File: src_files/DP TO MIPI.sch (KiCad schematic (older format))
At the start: 20 parts

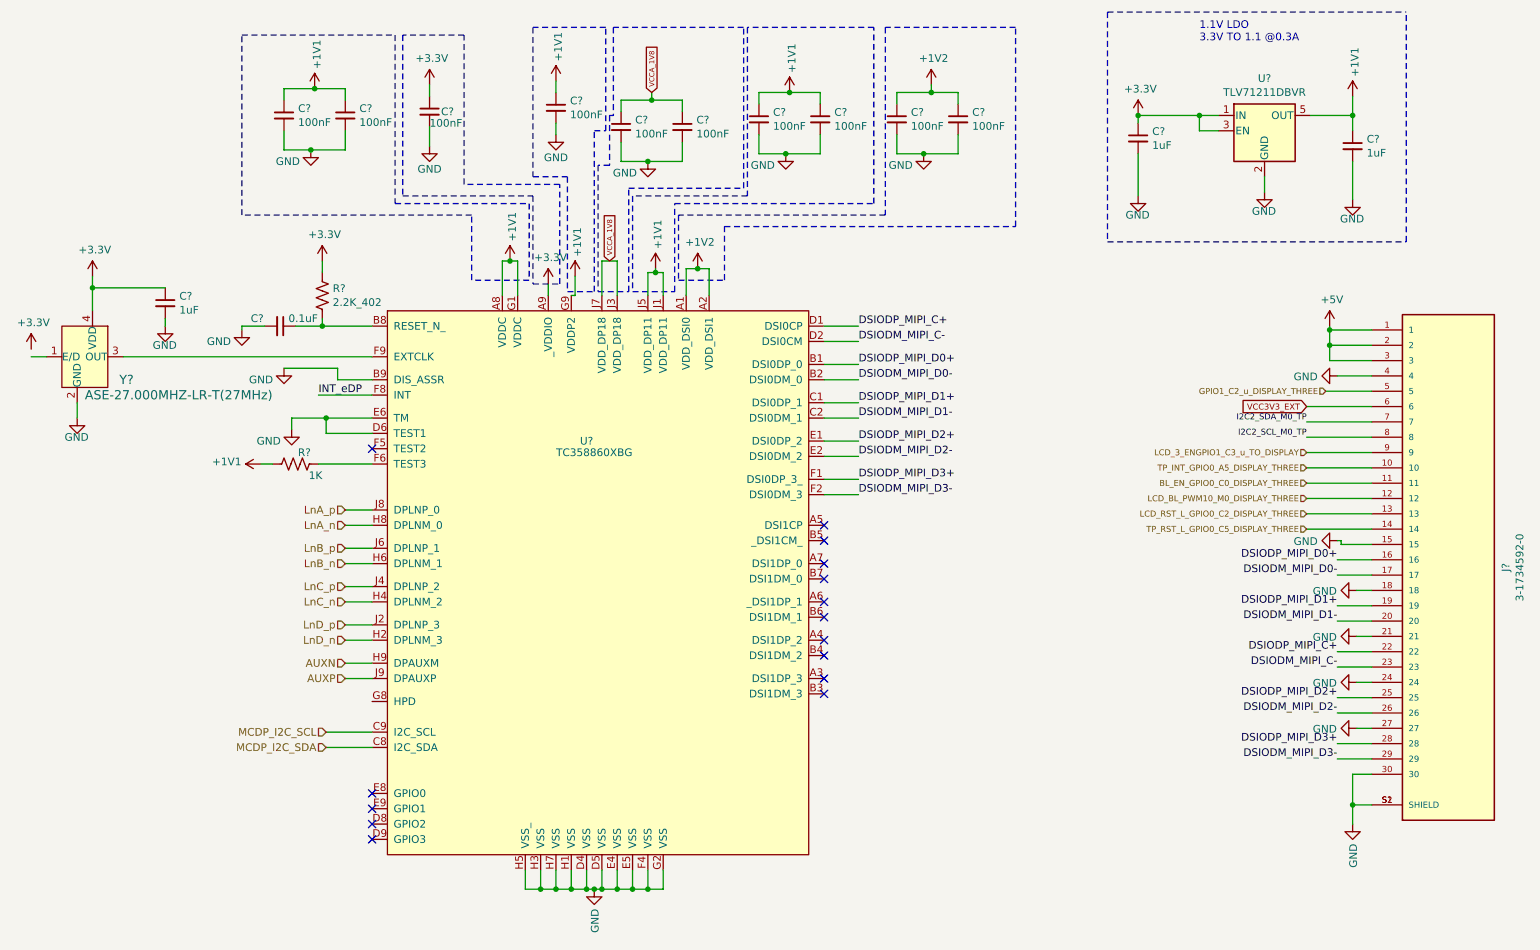
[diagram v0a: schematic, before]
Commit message: complete update on schematic and all display interfaces
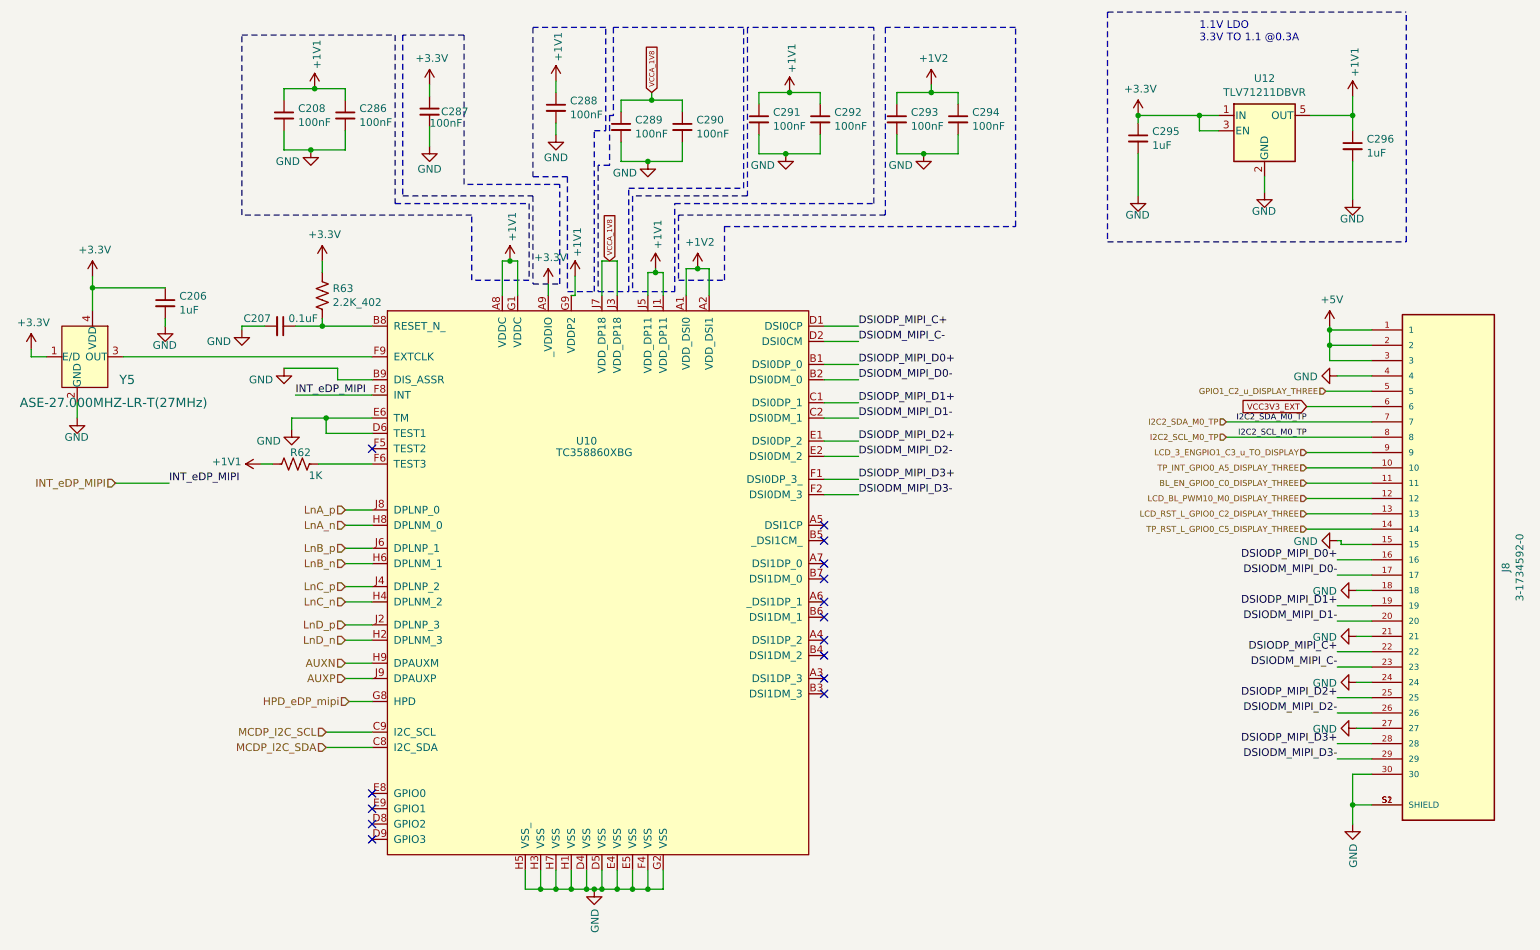
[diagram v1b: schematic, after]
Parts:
- gave numbers to parts that had none: 20
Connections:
- net +3V3: now also Y5.1 (E/D)
- net HPD_eDP_mipi: now reaches U10.G8 (HPD)
- net INT_eDP renamed INT_eDP_MIPI

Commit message: complete update on schematiC + FOOTPRINT
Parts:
- U10: footprint (none) -> greencharge-footprints:TC358860XBG
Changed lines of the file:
@@
 F 0 "U10" H 4375 50  50  0000 C CNN
 F 1 "TC358860XBG" H 4425 -25 50  0000 C CNN
-F 2 "" H 3375 1050 50  0001 C CNN
+F 2 "greencharge-footprints:TC358860XBG" H 3375 1050 50  0001 C CNN
 F 3 "" H 3375 1050 50  0001 C CNN
 	1    4375 1750
